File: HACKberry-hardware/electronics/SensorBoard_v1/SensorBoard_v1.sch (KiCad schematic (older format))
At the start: 4 parts, among them U1 3-CONDUCTOR_MINIATUIRE_JACK_M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, U2 TPR-105

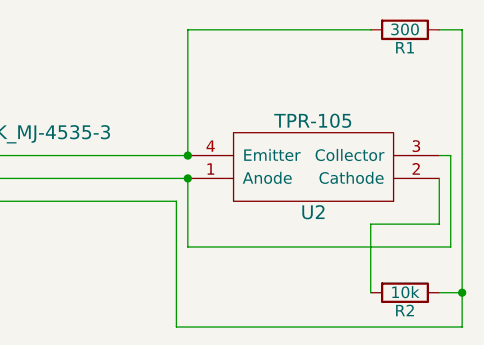
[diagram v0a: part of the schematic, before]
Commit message: Fixed an error of SensorBoard schematic
resistance values were not correct.
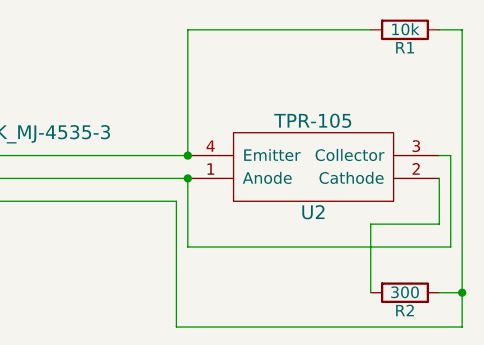
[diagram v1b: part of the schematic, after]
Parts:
- R1: value 300 -> 10k
- R2: value 10k -> 300
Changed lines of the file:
@@
 LIBS:contrib
 LIBS:valves
+LIBS:myParts
 LIBS:SensorBoard_v1-cache
 EELAYER 25 0
@@
 P 6950 3350
 F 0 "R1" V 7030 3350 50  0000 C CNN
-F 1 "300" V 6950 3350 50  0000 C CNN
+F 1 "10k" V 6950 3350 50  0000 C CNN
 F 2 "" V 6880 3350 30  0000 C CNN
 F 3 "" H 6950 3350 30  0000 C CNN
@@
 P 6950 4500
 F 0 "R2" V 7030 4500 50  0000 C CNN
-F 1 "10k" V 6950 4500 50  0000 C CNN
+F 1 "300" V 6950 4500 50  0000 C CNN
 F 2 "" V 6880 4500 30  0000 C CNN
 F 3 "" H 6950 4500 30  0000 C CNN

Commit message: Added presentation files
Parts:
- U1: symbol 3-CONDUCTOR_MINIATUIRE_JACK_MJ-4535-3 -> 3-CONDUCTOR_MINIATUIRE_JACK_MJ-4535-3-RESCUE-SensorBoard_v1
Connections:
- net at U2.1 (Anode), U2.3 (Collector): now also U1.4 (VCC); no longer U1.2 (VCC)
- net at R1.1, R2.1: now also U1.2 (GND); no longer U1.3 (GND)
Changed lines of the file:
@@
 EESchema Schematic File Version 2
+LIBS:SensorBoard_v1-rescue
 LIBS:power
 LIBS:device
@@
 $EndDescr
 $Comp
-L 3-CONDUCTOR_MINIATUIRE_JACK_MJ-4535-3 U1
+L 3-CONDUCTOR_MINIATUIRE_JACK_MJ-4535-3-RESCUE-SensorBoard_v1 U1
 U 1 1 55601F64
 P 4750 4000

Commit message: Added garber data of SensorBoard
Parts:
- removed U1: 3-CONDUCTOR_MINIATUIRE_JACK_MJ-4535-3, symbol 3-CONDUCTOR_MINIATUIRE_JACK_MJ-4535-3-RESCUE-SensorBoard_v1
- added U1: 3-CONDUCTOR_MINIATUIRE_JACK_MJ-4535-3-RESCUE-Hand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, HACKberry_v1:MINIATURE_JACK_MJ-4535-3, symbol 3-CONDUCTOR_MINIATUIRE_JACK_MJ-4535-3-RESCUE-HandBoard_v1
- R1, R2: footprint (none) -> Resistors_SMD:R_0603_HandSoldering
- U2: footprint (none) -> HACKberry_v1:TPR-105smd
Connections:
- net at R1.2, U2.4 (Emitter): now also U1.4 (INPUT)
- net at R1.1, R2.1: now also U1.1 (GND)
- net at U2.1 (Anode), U2.3 (Collector): now also U1.2 (VCC)
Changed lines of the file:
@@
 LIBS:myParts
 LIBS:SensorBoard_v1-cache
+LIBS:HACKberry_v1
 EELAYER 25 0
 EELAYER END
@@
 $EndDescr
 $Comp
-L 3-CONDUCTOR_MINIATUIRE_JACK_MJ-4535-3-RESCUE-SensorBoard_v1 U1
-U 1 1 55601F64
-P 4750 4000
-F 0 "U1" H 4550 4300 60  0000 C CNN
-F 1 "3-CONDUCTOR_MINIATUIRE_JACK_MJ-4535-3" H 4750 4200 60  0000 C CNN
-F 2 "" H 4750 4200 60  0000 C CNN
-F 3 "" H 4750 4200 60  0000 C CNN
-	1    4750 4000
-	1    0    0    -1
-$EndComp
-$Comp
 L TPR-105 U2
 U 1 1 55602C89
@@
 F 0 "U2" H 6550 4150 60  0000 C CNN
 F 1 "TPR-105" H 6550 3750 60  0000 C CNN
-F 2 "" H 6550 3950 60  0000 C CNN
+F 2 "HACKberry_v1:TPR-105smd" H 6550 3950 60  0001 C CNN
 F 3 "" H 6550 3950 60  0000 C CNN
 	1    6550 3950
@@
 F 0 "R1" V 7030 3350 50  0000 C CNN
 F 1 "10k" V 6950 3350 50  0000 C CNN
-F 2 "" V 6880 3350 30  0000 C CNN
+F 2 "Resistors_SMD:R_0603_HandSoldering" V 6880 3350 30  0001 C CNN
 F 3 "" H 6950 3350 30  0000 C CNN
 	1    6950 3350
@@
 F 0 "R2" V 7030 4500 50  0000 C CNN
 F 1 "300" V 6950 4500 50  0000 C CNN
-F 2 "" V 6880 4500 30  0000 C CNN
+F 2 "Resistors_SMD:R_0603_HandSoldering" V 6880 4500 30  0001 C CNN
 F 3 "" H 6950 4500 30  0000 C CNN
 	1    6950 4500
@@
 $EndComp
 Wire Wire Line
-	5100 3900 6000 3900
+	4650 3900 6000 3900
 Wire Wire Line
 	6800 3350 6000 3350
@@
 	6000 3350 6000 3900
 Wire Wire Line
-	5100 4000 6000 4000
+	4650 4000 6000 4000
 Wire Wire Line
 	7100 4000 7100 4200
@@
 	6000 4300 6000 4000
 Wire Wire Line
-	5100 4100 5950 4100
+	4650 4100 5950 4100
 Wire Wire Line
 	5950 4100 5950 4650
 Wire Wire Line
-	5950 4650 7200 4650
+	7200 4650 5950 4650
 Connection ~ 7200 4500
 Wire Wire Line
-	7200 4650 7200 3350
+	7200 3350 7200 4650
 Wire Wire Line
 	7150 3900 7150 4300
 Connection ~ 6000 3900
 Connection ~ 6000 4000
+$Comp
+L 3-CONDUCTOR_MINIATUIRE_JACK_MJ-4535-3-RESCUE-HandBoard_v1 U1
+U 1 1 55C4B6D8
+P 4300 4000
+F 0 "U1" H 4100 4300 60  0000 C CNN
+F 1 "3-CONDUCTOR_MINIATUIRE_JACK_MJ-4535-3-RESCUE-HandBoard_v1" H 4300 4200 60  0000 C CNN
+F 2 "HACKberry_v1:MINIATURE_JACK_MJ-4535-3" H 4300 4200 60  0001 C CNN
+F 3 "" H 4300 4200 60  0000 C CNN
+	1    4300 4000
+	1    0    0    -1
+$EndComp
 $EndSCHEMATC
